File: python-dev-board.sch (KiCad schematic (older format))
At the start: 36 parts, among them IC1 STM32F405RGT, J3 USB_OTG, SW1 SW_Push, Y1 8MHz, Y2 32.768KHz

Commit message: added pin headers to schematic
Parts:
- added J1, J2: Conn_01x17, Pin_Headers:Pin_Header_Straight_1x17_Pitch2.54mm, symbol Conn_01x17
- J4: renamed from J?; footprint MOLEX_503182-1852 -> my_footprints:molex_sd_47309-2851
- gave numbers to parts that had none: 1
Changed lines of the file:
@@
 LIBS:contrib
 LIBS:valves
-LIBS:minibuoy_v1-cache
 LIBS:ws2812b
 LIBS:python-dev-board-cache
@@
 DFU boot
 $Comp
-L +3V3 #+3V2
+L +3V3 #+3V01
 U 1 1 5B40BCA4
 P 6350 3450
-F 0 "#+3V2" V 6250 3250 70  0001 L BNN
+F 0 "#+3V01" V 6250 3250 70  0001 L BNN
 F 1 "+3V3" V 6250 3250 70  0000 L BNN
 F 2 "" H 6350 3450 60  0001 C CNN
@@
 $EndComp
 $Comp
-L GND #GND5
+L GND #GND02
 U 1 1 5B40BCA5
 P 5650 4950
-F 0 "#GND5" H 5550 4850 70  0001 L BNN
+F 0 "#GND02" H 5550 4850 70  0001 L BNN
 F 1 "GND" V 5550 4850 70  0000 L BNN
 F 2 "" H 5650 4950 60  0001 C CNN
@@
 $EndComp
 $Comp
-L GND #GND6
+L GND #GND03
 U 1 1 5B40BCA6
 P 6050 4950
-F 0 "#GND6" H 5950 4850 70  0001 L BNN
+F 0 "#GND03" H 5950 4850 70  0001 L BNN
 F 1 "GND" V 5950 4850 70  0000 L BNN
 F 2 "" H 6050 4950 60  0001 C CNN
@@
 $EndComp
 $Comp
-L GND #GND1
+L GND #GND04
 U 1 1 5B40BCA7
 P 4850 5850
-F 0 "#GND1" H 4750 5750 70  0001 L BNN
+F 0 "#GND04" H 4750 5750 70  0001 L BNN
 F 1 "GND" H 4750 5650 70  0000 L BNN
 F 2 "" H 4850 5850 60  0001 C CNN
@@
 $EndComp
 $Comp
-L GND #GND4
+L GND #GND05
 U 1 1 5B40BCA8
 P 5250 4950
-F 0 "#GND4" H 5150 4850 70  0001 L BNN
+F 0 "#GND05" H 5150 4850 70  0001 L BNN
 F 1 "GND" V 5150 4850 70  0000 L BNN
 F 2 "" H 5250 4950 60  0001 C CNN
@@
 $EndComp
 $Comp
-L GND #GND2
+L GND #GND06
 U 1 1 5B40BCA9
 P 4850 6850
-F 0 "#GND2" H 4750 6750 70  0001 L BNN
+F 0 "#GND06" H 4750 6750 70  0001 L BNN
 F 1 "GND" H 4750 6650 70  0000 L BNN
 F 2 "" H 4850 6850 60  0001 C CNN
@@
 $EndComp
 $Comp
-L GND #GND3
+L GND #GND07
 U 1 1 5B40BCAA
 P 5100 10800
-F 0 "#GND3" H 5000 10700 70  0001 L BNN
+F 0 "#GND07" H 5000 10700 70  0001 L BNN
 F 1 "GND" V 5000 10700 70  0000 L BNN
 F 2 "" H 5100 10800 60  0001 C CNN
@@
 INA219_HSD_SW
 $Comp
-L +BATT #PWR3
+L +BATT #PWR08
 U 1 1 5B40BCB8
 P 9600 1150
-F 0 "#PWR3" H 9600 1000 50  0001 C CNN
+F 0 "#PWR08" H 9600 1000 50  0001 C CNN
 F 1 "+BATT" H 9600 1290 50  0000 C CNN
 F 2 "" H 9600 1150 50  0001 C CNN
@@
 $EndComp
 $Comp
-L GND #PWR4
+L GND #PWR09
 U 1 1 5B40BCB9
 P 10100 1850
-F 0 "#PWR4" H 10100 1600 50  0001 C CNN
+F 0 "#PWR09" H 10100 1600 50  0001 C CNN
 F 1 "GND" H 10100 1700 50  0000 C CNN
 F 2 "" H 10100 1850 50  0001 C CNN
@@
 $EndComp
 $Comp
-L +3V3 #+3V5
+L +3V3 #+3V010
 U 1 1 5B40BCBA
 P 10800 1150
-F 0 "#+3V5" V 10700 950 70  0001 L BNN
+F 0 "#+3V010" V 10700 950 70  0001 L BNN
 F 1 "+3V3" H 10700 1300 70  0000 L BNN
 F 2 "" H 10800 1150 60  0001 C CNN
@@
 FS_USB_ID
 $Comp
-L GND #PWR7
+L GND #PWR011
 U 1 1 5B40BCC1
 P 12400 4150
-F 0 "#PWR7" H 12400 3900 50  0001 C CNN
+F 0 "#PWR011" H 12400 3900 50  0001 C CNN
 F 1 "GND" H 12400 4000 50  0000 C CNN
 F 2 "" H 12400 4150 50  0001 C CNN
@@
 $EndComp
 $Comp
-L GND #PWR9
+L GND #PWR012
 U 1 1 5B40BCC3
 P 13800 6900
-F 0 "#PWR9" H 13800 6650 50  0001 C CNN
+F 0 "#PWR012" H 13800 6650 50  0001 C CNN
 F 1 "GND" H 13800 6750 50  0000 C CNN
 F 2 "" H 13800 6900 50  0001 C CNN
@@
 $EndComp
 $Comp
-L GND #PWR10
+L GND #PWR013
 U 1 1 5B40BCC4
 P 14550 6900
-F 0 "#PWR10" H 14550 6650 50  0001 C CNN
+F 0 "#PWR013" H 14550 6650 50  0001 C CNN
 F 1 "GND" H 14550 6750 50  0000 C CNN
 F 2 "" H 14550 6900 50  0001 C CNN
@@
 $EndComp
 $Comp
-L +3V3 #+3V8
+L +3V3 #+3V014
 U 1 1 5B40BCC7
 P 14550 5950
-F 0 "#+3V8" V 14450 5750 70  0001 L BNN
+F 0 "#+3V014" V 14450 5750 70  0001 L BNN
 F 1 "+3V3" V 14450 5750 70  0000 L BNN
 F 2 "" H 14550 5950 60  0001 C CNN
@@
 $EndComp
 $Comp
-L GND #PWR8
+L GND #PWR015
 U 1 1 5B40BCC9
 P 13750 7800
-F 0 "#PWR8" H 13750 7550 50  0001 C CNN
+F 0 "#PWR015" H 13750 7550 50  0001 C CNN
 F 1 "GND" H 13750 7650 50  0000 C CNN
 F 2 "" H 13750 7800 50  0001 C CNN
@@
 $EndComp
 $Comp
-L +3V3 #+3V9
+L +3V3 #+3V016
 U 1 1 5B40BCD4
 P 14950 8000
-F 0 "#+3V9" V 14850 7800 70  0001 L BNN
+F 0 "#+3V016" V 14850 7800 70  0001 L BNN
 F 1 "+3V3" V 14850 7800 70  0000 L BNN
 F 2 "" H 14950 8000 60  0001 C CNN
@@
 $EndComp
 $Comp
-L GND #PWR6
+L GND #PWR017
 U 1 1 5B40BCD5
 P 12100 1700
-F 0 "#PWR6" H 12100 1450 50  0001 C CNN
+F 0 "#PWR017" H 12100 1450 50  0001 C CNN
 F 1 "GND" H 12100 1550 50  0000 C CNN
 F 2 "" H 12100 1700 50  0001 C CNN
@@
 $EndComp
 $Comp
-L +3V3 #+3V7
+L +3V3 #+3V018
 U 1 1 5B40BCDA
 P 12100 1150
-F 0 "#+3V7" V 12000 950 70  0001 L BNN
+F 0 "#+3V018" V 12000 950 70  0001 L BNN
 F 1 "+3V3" H 12000 1300 70  0000 L BNN
 F 2 "" H 12100 1150 60  0001 C CNN
@@
 SDIO_D0
 $Comp
-L GND #PWR1
+L GND #PWR019
 U 1 1 5B40BCDC
 P 8550 10450
-F 0 "#PWR1" H 8550 10200 50  0001 C CNN
+F 0 "#PWR019" H 8550 10200 50  0001 C CNN
 F 1 "GND" H 8550 10300 50  0000 C CNN
 F 2 "" H 8550 10450 50  0001 C CNN
@@
 	9200 10150 9450 10150
 $Comp
-L GND #PWR2
+L GND #PWR020
 U 1 1 5B40BCDD
 P 9250 10700
-F 0 "#PWR2" H 9250 10450 50  0001 C CNN
+F 0 "#PWR020" H 9250 10450 50  0001 C CNN
 F 1 "GND" H 9250 10550 50  0000 C CNN
 F 2 "" H 9250 10700 50  0001 C CNN
@@
 $EndComp
 $Comp
-L +3V3 #+3V6
+L +3V3 #+3V021
 U 1 1 5B40BCE2
 P 11250 6200
-F 0 "#+3V6" V 11150 6000 70  0001 L BNN
+F 0 "#+3V021" V 11150 6000 70  0001 L BNN
 F 1 "+3V3" V 11150 6000 70  0000 L BNN
 F 2 "" H 11250 6200 60  0001 C CNN
@@
 GPS_TX
 $Comp
-L +3V3 #+3V1
+L +3V3 #+3V022
 U 1 1 5B40BCE3
 P 6000 6350
-F 0 "#+3V1" V 5900 6150 70  0001 L BNN
+F 0 "#+3V022" V 5900 6150 70  0001 L BNN
 F 1 "+3V3" V 5900 6150 70  0000 L BNN
 F 2 "" H 6000 6350 60  0001 C CNN
@@
 	6000 6500 6000 6350
 $Comp
-L +3V3 #+3V3
+L +3V3 #+3V023
 U 1 1 5B4E5B17
 P 8500 9550
-F 0 "#+3V3" V 8400 9350 70  0001 L BNN
+F 0 "#+3V023" V 8400 9350 70  0001 L BNN
 F 1 "+3V3" V 8400 9350 70  0000 L BNN
 F 2 "" H 8500 9550 60  0001 C CNN
@@
 $EndComp
 $Comp
-L +3V3 #+3V4
+L +3V3 #+3V024
 U 1 1 5B4E6D6D
 P 10700 2550
-F 0 "#+3V4" V 10600 2350 70  0001 L BNN
+F 0 "#+3V024" V 10600 2350 70  0001 L BNN
 F 1 "+3V3" V 10600 2350 70  0000 L BNN
 F 2 "" H 10700 2550 60  0001 C CNN
@@
 $EndComp
 $Comp
-L GND #PWR5
+L GND #PWR025
 U 1 1 5B4E6DE4
 P 12000 3150
-F 0 "#PWR5" H 12000 2900 50  0001 C CNN
+F 0 "#PWR025" H 12000 2900 50  0001 C CNN
 F 1 "GND" H 12000 3000 50  0000 C CNN
 F 2 "" H 12000 3150 50  0001 C CNN
@@
 	11900 2650 12150 2650
 $Comp
-L LM1117-3.3 U?
+L LM1117-3.3 U1
 U 1 1 5B590D19
 P 10100 1300
-F 0 "U?" H 9950 1425 50  0000 C CNN
+F 0 "U1" H 9950 1425 50  0000 C CNN
 F 1 "LM1117-3.3" H 10100 1425 50  0000 L CNN
 F 2 "TO_SOT_Packages_SMD:SOT-223-3Lead_TabPin2" H 10100 1300 50  0001 C CNN
@@
 $EndComp
 $Comp
-L 47309-2851 J?
+L 47309-2851 J4
 U 1 1 5B594E99
 P 9650 10050
-F 0 "J?" H 9650 10773 50  0000 L BNN
+F 0 "J4" H 9650 10773 50  0000 L BNN
 F 1 "47309-2851" H 9650 9226 50  0000 L BNN
-F 2 "MOLEX_503182-1852" H 9600 10950 50  0001 L BNN
+F 2 "my_footprints:molex_sd_47309-2851" H 9600 10950 50  0001 L BNN
 F 3 "503182-1852" H 9750 10900 50  0001 L BNN
 F 4 "Good" H 9650 10050 50  0001 L BNN "Field4"
@@
 	1    0    0    -1
 $EndComp
+$Comp
+L Conn_01x17 J2
+U 1 1 5B5BA56D
+P 3750 8650
+F 0 "J2" H 3750 9550 50  0000 C CNN
+F 1 "Conn_01x17" H 3750 7750 50  0000 C CNN
+F 2 "Pin_Headers:Pin_Header_Straight_1x17_Pitch2.54mm" H 3750 8650 50  0001 C CNN
+F 3 "" H 3750 8650 50  0001 C CNN
+	1    3750 8650
+	1    0    0    -1
+$EndComp
+$Comp
+L Conn_01x17 J1
+U 1 1 5B5BABA7
+P 2200 8650
+F 0 "J1" H 2200 9550 50  0000 C CNN
+F 1 "Conn_01x17" H 2200 7750 50  0000 C CNN
+F 2 "Pin_Headers:Pin_Header_Straight_1x17_Pitch2.54mm" H 2200 8650 50  0001 C CNN
+F 3 "" H 2200 8650 50  0001 C CNN
+	1    2200 8650
+	-1   0    0    1
+$EndComp
 $EndSCHEMATC

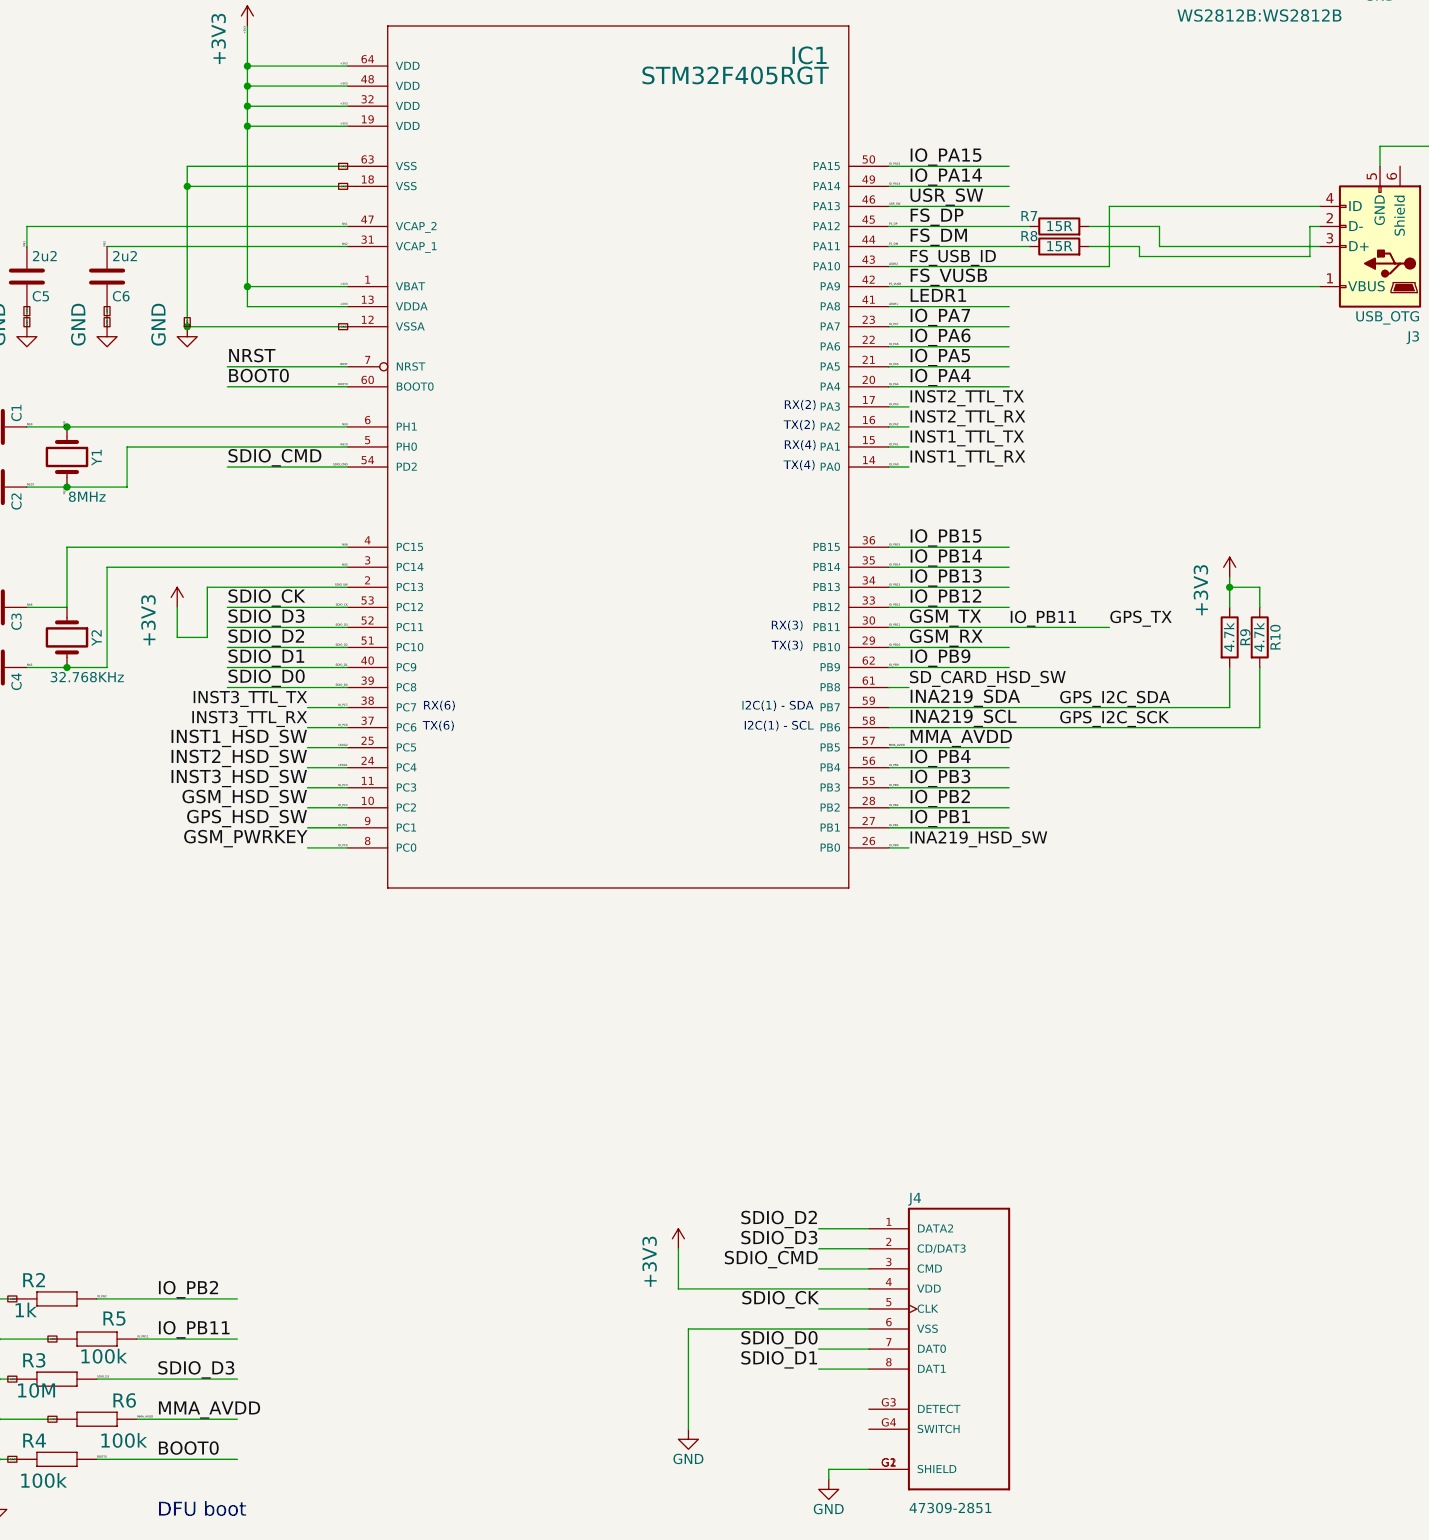
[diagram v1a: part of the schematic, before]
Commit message: shortened pin names on schematic
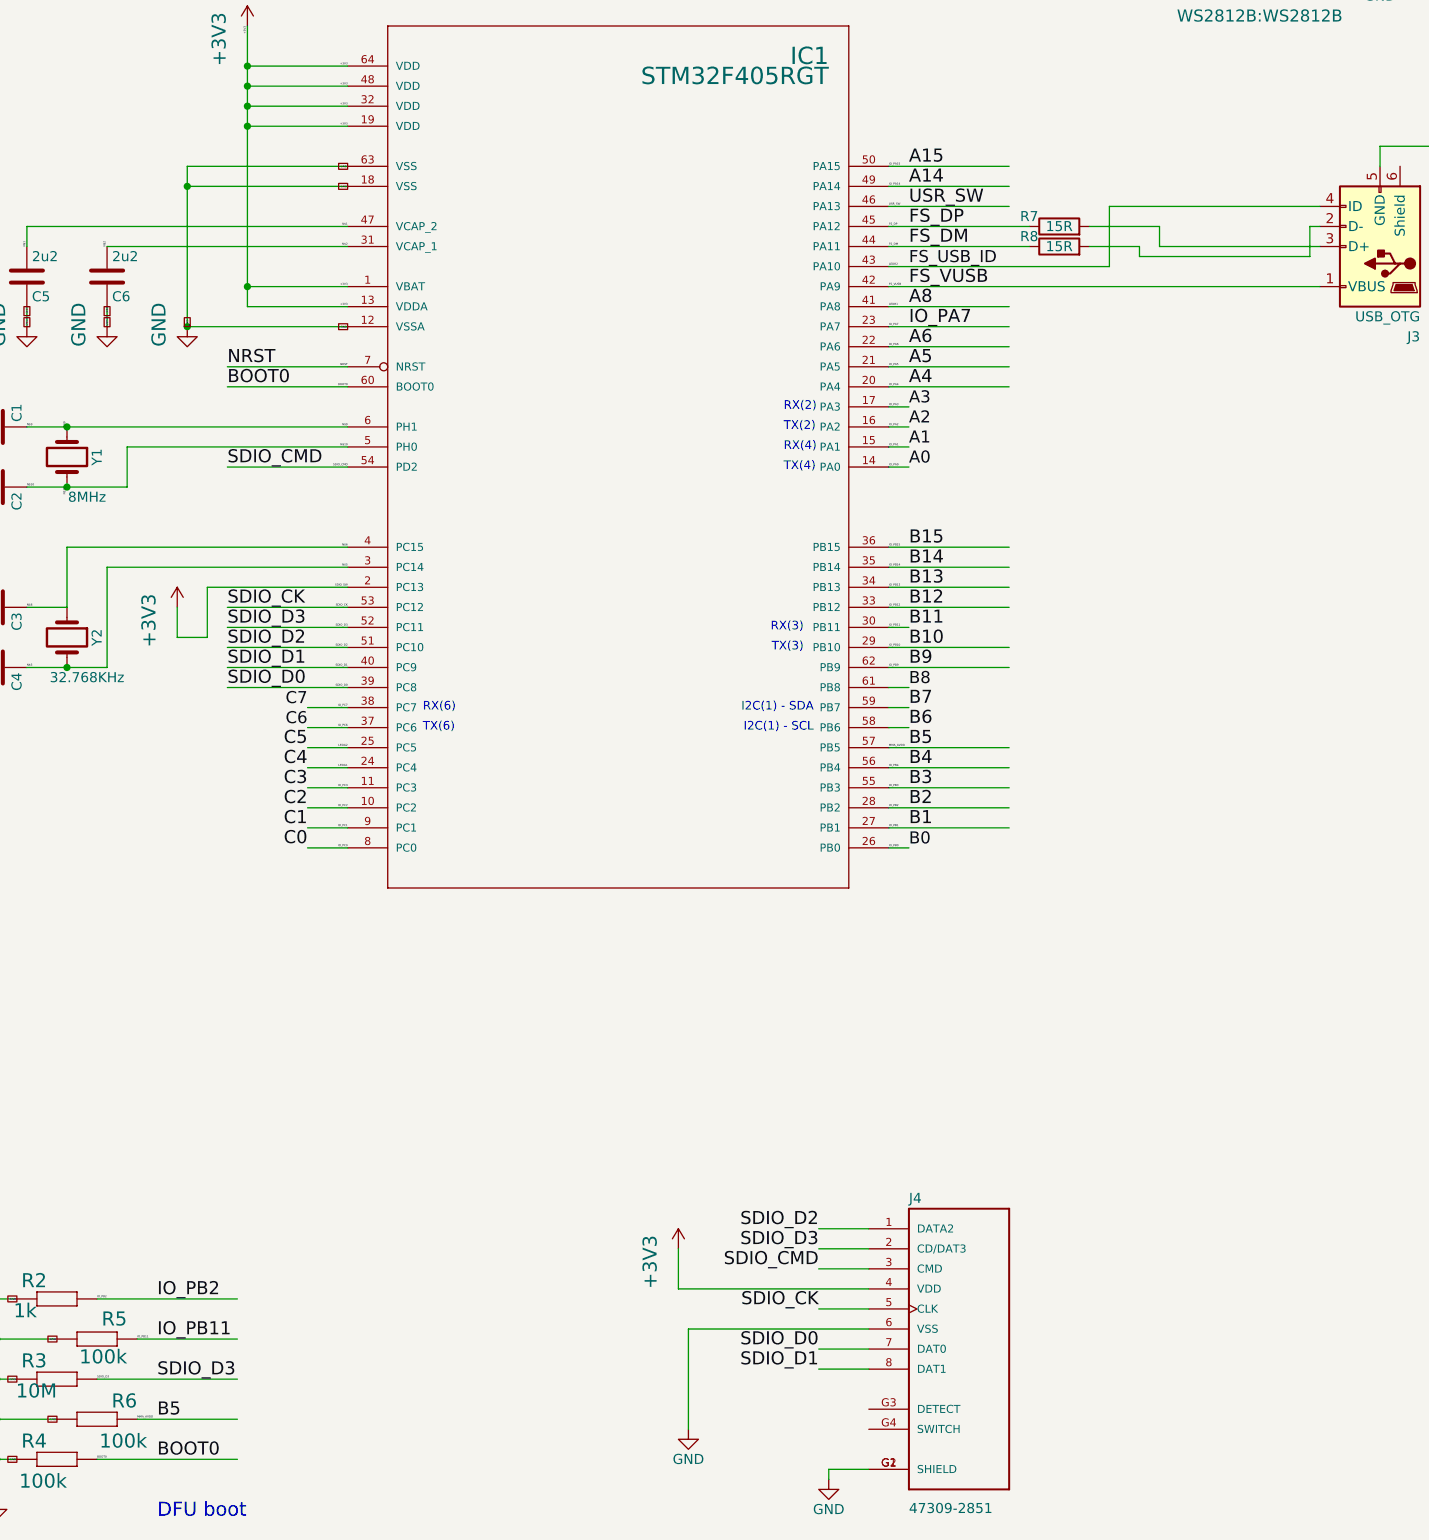
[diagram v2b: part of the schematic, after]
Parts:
- removed R10, R9: 4.7k, Resistors_SMD:R_0603, symbol R
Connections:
- net labels added: A0, A1, A14, A15, A2, A3, A4, A5, A6, A8, B0, B1, B10, B11, B12, B13, B14, B15, B2, B3, B4, B5, B6, B7, B8, B9, C0, C1, C2, C3, C4, C5, C6, C7
- net labels removed: GPS_HSD_SW, GPS_I2C_SCK, GPS_I2C_SDA, GPS_TX, GSM_HSD_SW, GSM_PWRKEY, GSM_RX, GSM_TX, INA219_HSD_SW, INA219_SCL, INA219_SDA, INST1_HSD_SW, INST1_TTL_RX, INST1_TTL_TX, INST2_HSD_SW, INST2_TTL_RX, INST2_TTL_TX, INST3_HSD_SW, INST3_TTL_RX, INST3_TTL_TX, SD_CARD_HSD_SW
- wire segments 159 -> 154
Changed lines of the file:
@@
 FS_VUSB
 Text Label 9650 5250 0    65   ~ 0
-IO_PA4
+A4
 Text Label 9650 5150 0    65   ~ 0
-IO_PA5
+A5
 Text Label 9650 5050 0    65   ~ 0
-IO_PA6
+A6
 Text Label 9650 4950 0    65   ~ 0
 IO_PA7
 Text Label 9650 4250 0    65   ~ 0
-IO_PA14
+A14
 Text Label 9650 4150 0    65   ~ 0
-IO_PA15
+A15
 Text Label 9650 7450 0    65   ~ 0
-IO_PB1
+B1
 Text Label 9650 7350 0    65   ~ 0
-IO_PB2
+B2
 Text Label 5900 9800 0    65   ~ 0
 IO_PB2
 Text Label 9650 7250 0    65   ~ 0
-IO_PB3
+B3
 Text Label 9650 7150 0    65   ~ 0
-IO_PB4
+B4
 Text Label 9650 6650 0    65   ~ 0
-IO_PB9
+B9
 Text Label 5900 10000 0    65   ~ 0
 IO_PB11
 Text Label 9650 6350 0    65   ~ 0
-IO_PB12
+B12
 Text Label 9650 6250 0    65   ~ 0
-IO_PB13
+B13
 Text Label 9650 6150 0    65   ~ 0
-IO_PB14
+B14
 Text Label 9650 6050 0    65   ~ 0
-IO_PB15
+B15
 Text Label 6650 7550 2    65   ~ 0
-GSM_PWRKEY
+C0
 Text Label 9650 4850 0    65   ~ 0
-LEDR1
+A8
 Text Label 9650 7050 0    65   ~ 0
-MMA_AVDD
+B5
 Text Label 5900 10400 0    65   ~ 0
-MMA_AVDD
+B5
 Text Label 6250 5150 0    65   ~ 0
 NRST
@@
 USR_SW
 Text Label 9650 5550 0    60   ~ 0
-INST1_TTL_TX
+A1
 Text Label 9650 5650 0    60   ~ 0
-INST1_TTL_RX
+A0
 Text Notes 9025 5675 0    43   ~ 0
 TX(4)
@@
 RX(2)
 Text Label 9650 5350 0    60   ~ 0
-INST2_TTL_TX
+A3
 Text Label 9650 5450 0    60   ~ 0
-INST2_TTL_RX
+A2
 Text Notes 7225 6975 0    43   ~ 0
 TX(6)
@@
 RX(6)
 Text Label 6650 6850 2    60   ~ 0
-INST3_TTL_TX
+C7
 Text Label 6650 6950 2    60   ~ 0
-INST3_TTL_RX
+C6
 Text Notes 9175 6975 2    43   ~ 0
 I2C(1) - SCL
@@
 I2C(1) - SDA
 Text Label 9650 6950 0    65   ~ 0
-INA219_SCL
+B6
 Text Label 9650 6850 0    65   ~ 0
-INA219_SDA
+B7
 Text Label 6650 7050 2    65   ~ 0
-INST1_HSD_SW
+C5
 Text Label 6650 7150 2    65   ~ 0
-INST2_HSD_SW
+C4
 Text Label 6650 7250 2    65   ~ 0
-INST3_HSD_SW
+C3
 Text Label 6650 7350 2    65   ~ 0
-GSM_HSD_SW
+C2
 Text Label 6650 7450 2    65   ~ 0
-GPS_HSD_SW
+C1
 Text Label 9650 6450 0    65   ~ 0
-GSM_TX
+B11
 Text Label 9650 6550 0    65   ~ 0
-GSM_RX
+B10
 Text Notes 9125 6575 2    43   ~ 0
 TX(3)
@@
 GND
 Text Label 9650 7550 0    60   ~ 0
-INA219_HSD_SW
+B0
 $Comp
 L +BATT #PWR08
@@
 $EndComp
 Text Label 9650 6750 0    60   ~ 0
-SD_CARD_HSD_SW
+B8
 $Comp
 L USB_OTG J3
@@
 	6650 6950 6850 6950
 Wire Wire Line
-	9550 6950 11400 6950
-Wire Wire Line
-	9550 6850 11250 6850
-Wire Wire Line
 	6650 7050 6850 7050
 Wire Wire Line
@@
 Wire Wire Line
 	9550 6550 10150 6550
-Wire Wire Line
-	9550 6450 10650 6450
 Wire Wire Line
 	6650 7550 6850 7550
@@
 Wire Wire Line
 	12100 1250 12100 1150
-Text Label 10150 6450 0    60   ~ 0
-IO_PB11
 Text Label 9200 9650 2    65   ~ 0
 SDIO_CMD
@@
 Wire Wire Line
 	5450 6350 5450 6050
-Text Label 10400 6850 0    60   ~ 0
-GPS_I2C_SDA
-Text Label 10400 6950 0    60   ~ 0
-GPS_I2C_SCK
-Wire Wire Line
-	11250 6850 11250 6650
-Wire Wire Line
-	11400 6950 11400 6650
-$Comp
-L R R9
-U 1 1 5B40BCE0
-P 11250 6500
-F 0 "R9" V 11330 6500 50  0000 C CNN
-F 1 "4.7k" V 11250 6500 50  0000 C CNN
-F 2 "Resistors_SMD:R_0603" V 11180 6500 50  0001 C CNN
-F 3 "" H 11250 6500 50  0001 C CNN
-	1    11250 6500
-	1    0    0    -1
-$EndComp
-$Comp
-L R R10
-U 1 1 5B40BCE1
-P 11400 6500
-F 0 "R10" V 11480 6500 50  0000 C CNN
-F 1 "4.7k" V 11400 6500 50  0000 C CNN
-F 2 "Resistors_SMD:R_0603" V 11330 6500 50  0001 C CNN
-F 3 "" H 11400 6500 50  0001 C CNN
-	1    11400 6500
-	1    0    0    -1
-$EndComp
-$Comp
-L +3V3 #+3V021
-U 1 1 5B40BCE2
-P 11250 6200
-F 0 "#+3V021" V 11150 6000 70  0001 L BNN
-F 1 "+3V3" V 11150 6000 70  0000 L BNN
-F 2 "" H 11250 6200 60  0001 C CNN
-F 3 "" H 11250 6200 60  0001 C CNN
-	1    11250 6200
-	1    0    0    -1
-$EndComp
-Wire Wire Line
-	11400 6350 11400 6250
-Wire Wire Line
-	11400 6250 11250 6250
-Wire Wire Line
-	11250 6200 11250 6350
-Connection ~ 11250 6250
-Text Label 10650 6450 0    60   ~ 0
-GPS_TX
 $Comp
 L +3V3 #+3V022
@@
 	-1   0    0    1
 $EndComp
+Wire Wire Line
+	9550 6850 9650 6850
+Wire Wire Line
+	9550 6950 9650 6950
+Wire Wire Line
+	9550 6450 9650 6450
 $EndSCHEMATC
